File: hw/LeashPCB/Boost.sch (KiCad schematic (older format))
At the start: 38 parts, among them U1001 TPS62821DLC, U1002 TPS61026, U1003 TPS61025

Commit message: Added antenna and routed ideal diode circuit
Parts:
- removed JP801, JP802, JP804, JP805, JP806: SolderJumper_2_Bridged, Jumper:SolderJumper-2_P1.3mm_Bridged2Bar_RoundedPad1.0x1.5mm, symbol Jumper:SolderJumper_2_Bridged
- removed JP803: SolderJumper_2_Open, Jumper:SolderJumper-2_P1.3mm_Open_RoundedPad1.0x1.5mm, symbol Jumper:SolderJumper_2_Open
- added R10, R9: 0, Resistor_SMD:R_0402_1005Metric, symbol Device:R
- C1003, C1007, L1003, R1008, R1014, R1015, U1001: Population (none) -> DNP
- C1009: footprint Capacitor_SMD:C_0402_1005Metric -> Capacitor_SMD:C_0603_1608Metric; Population (none) -> DNP
- R1017: Population DNP -> (none)
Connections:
- net labels added: +3V3, +5V, 3V3_BOOST_VOUT, 3V3_BUCK_VOUT, 5V_BOOST_VOUT
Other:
- note added: "Not normally populated"
- moved on the sheet: C1003, C1007, C1009, L1003, R1008, R1014, R1015

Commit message: Pulled in final small components and finished routing all but the RF section
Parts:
- added JP801, JP802, JP803, JP804, JP805: SolderJumper_2_Bridged, Jumper:SolderJumper-2_P1.3mm_Bridged2Bar_RoundedPad1.0x1.5mm, symbol Jumper:SolderJumper_2_Bridged
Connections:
- wire segments 161 -> 166
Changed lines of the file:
@@
 $EndComp
 Connection ~ 8800 7500
-Text HLabel 2125 2100 0    98   Input ~ 0
+Text HLabel 1475 2100 0    98   Input ~ 0
 V_BAT
-Text HLabel 2125 2375 0    98   Input ~ 0
+Text HLabel 1475 2375 0    98   Input ~ 0
 V_ALT
 Wire Wire Line
 	3775 7500 4725 7500
-Text HLabel 2125 2675 0    98   Input ~ 0
+Text HLabel 1475 2675 0    98   Input ~ 0
 V_USB
 Text HLabel 10025 2925 2    118  Input ~ 0
@@
 3V3_REG
 Wire Wire Line
-	2125 2100 2600 2100
-Wire Wire Line
-	2125 2375 2300 2375
-Wire Wire Line
 	3100 2375 3100 2100
 Connection ~ 3100 2100
@@
 	3100 2100 3250 2100
 Wire Wire Line
-	2125 2675 2450 2675
-Wire Wire Line
 	3250 2675 3250 2100
 Connection ~ 3250 2100
-Wire Wire Line
-	2300 4875 2450 4875
-Connection ~ 2450 4875
-Wire Wire Line
-	2450 4875 2600 4875
 Text Notes 2975 3875 0    98   ~ 0
 V_Bat not hooked into \n5V output normally
@@
 Text Label 2925 4875 0    50   ~ 0
 5V_BOOST_VIN
-Connection ~ 2300 2375
-Connection ~ 2450 2675
 Connection ~ 2600 2100
 Wire Wire Line
@@
 Wire Wire Line
 	13800 4600 14150 4600
-Wire Wire Line
-	2450 2675 2450 4875
-Wire Wire Line
-	2300 2375 2300 4875
 $Comp
 L Device:R R10
@@
 $EndComp
 Wire Wire Line
-	2600 2100 3100 2100
-Wire Wire Line
-	2300 2375 3100 2375
-Wire Wire Line
-	2450 2675 3250 2675
+	2600 2100 2675 2100
 Wire Notes Line
 	10375 6850 10375 8875
@@
 Text Notes 5775 9025 0    98   ~ 0
 Not normally populated
+Wire Wire Line
+	2325 2375 2325 4050
+Connection ~ 2325 2375
+Wire Wire Line
+	2325 2375 2675 2375
+Wire Wire Line
+	2325 4875 2475 4875
+Wire Wire Line
+	2475 2675 2475 3750
+Connection ~ 2475 2675
+Wire Wire Line
+	2475 2675 2675 2675
+Connection ~ 2475 4875
+Wire Wire Line
+	2475 4875 2600 4875
+$Comp
+L Jumper:SolderJumper_2_Bridged JP803
+U 1 1 5D5C1D3B
+P 2825 2100
+F 0 "JP803" H 2825 2213 50  0000 C CNN
+F 1 "SolderJumper_2_Bridged" H 2825 2214 50  0001 C CNN
+F 2 "Jumper:SolderJumper-2_P1.3mm_Bridged2Bar_RoundedPad1.0x1.5mm" H 2825 2100 50  0001 C CNN
+F 3 "~" H 2825 2100 50  0001 C CNN
+	1    2825 2100
+	1    0    0    -1
+$EndComp
+$Comp
+L Jumper:SolderJumper_2_Bridged JP804
+U 1 1 5D5CEF43
+P 2825 2375
+F 0 "JP804" H 2825 2488 50  0000 C CNN
+F 1 "SolderJumper_2_Bridged" H 2825 2489 50  0001 C CNN
+F 2 "Jumper:SolderJumper-2_P1.3mm_Bridged2Bar_RoundedPad1.0x1.5mm" H 2825 2375 50  0001 C CNN
+F 3 "~" H 2825 2375 50  0001 C CNN
+	1    2825 2375
+	1    0    0    -1
+$EndComp
+$Comp
+L Jumper:SolderJumper_2_Bridged JP805
+U 1 1 5D5CF3F5
+P 2825 2675
+F 0 "JP805" H 2825 2788 50  0000 C CNN
+F 1 "SolderJumper_2_Bridged" H 2825 2789 50  0001 C CNN
+F 2 "Jumper:SolderJumper-2_P1.3mm_Bridged2Bar_RoundedPad1.0x1.5mm" H 2825 2675 50  0001 C CNN
+F 3 "~" H 2825 2675 50  0001 C CNN
+	1    2825 2675
+	1    0    0    -1
+$EndComp
+$Comp
+L Jumper:SolderJumper_2_Bridged JP802
+U 1 1 5D5CFDCF
+P 2475 3900
+F 0 "JP802" V 2475 4100 50  0000 L CNN
+F 1 "SolderJumper_2_Bridged" H 2475 4014 50  0001 C CNN
+F 2 "Jumper:SolderJumper-2_P1.3mm_Bridged2Bar_RoundedPad1.0x1.5mm" H 2475 3900 50  0001 C CNN
+F 3 "~" H 2475 3900 50  0001 C CNN
+	1    2475 3900
+	0    1    1    0
+$EndComp
+Wire Wire Line
+	2475 4050 2475 4875
+$Comp
+L Jumper:SolderJumper_2_Bridged JP801
+U 1 1 5D5D22C0
+P 2325 4200
+F 0 "JP801" V 2325 4525 50  0000 L CNN
+F 1 "SolderJumper_2_Bridged" H 2325 4314 50  0001 C CNN
+F 2 "Jumper:SolderJumper-2_P1.3mm_Bridged2Bar_RoundedPad1.0x1.5mm" H 2325 4200 50  0001 C CNN
+F 3 "~" H 2325 4200 50  0001 C CNN
+	1    2325 4200
+	0    1    1    0
+$EndComp
+Wire Wire Line
+	2325 4350 2325 4875
+Text Label 1625 2675 0    50   ~ 0
+V_USB
+Text Label 1625 2375 0    50   ~ 0
+V_ALT
+Text Label 1625 2100 0    50   ~ 0
+V_BAT
+Wire Wire Line
+	2975 2100 3100 2100
+Wire Wire Line
+	2975 2375 3100 2375
+Wire Wire Line
+	2975 2675 3250 2675
+Wire Wire Line
+	1475 2100 2600 2100
+Wire Wire Line
+	1475 2375 2325 2375
+Wire Wire Line
+	1475 2675 2475 2675
 $EndSCHEMATC

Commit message: Added a swtich for future testing that would allow us to remove the ideal diode controller
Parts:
- added R? (x3): 0, Resistor_SMD:R_0402_1005Metric, symbol Device:R
- added SW?: SW_SPDT, symbol Switch:SW_SPDT
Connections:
- wire segments 166 -> 181
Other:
- note added: "Adding in a low cost, small switch for\nfuture cost reduction. Removes the need\nfor ideal diode controller."
- note added: "CONFIG 1: All power inputs go into 3V3 boost, ALT and USB go into the 5V boost\nCONFIG 2: All power inputs go into 3V3 boost, all go into the 5V boost\nCONFIG 3: All power inputs go into 5V boost, 5V is bucked down to 3V3\nCONFIG 4: User has to manually swich from internal power to external power, which are diode ORed together"
- note removed: "CONFIG 1: All power inputs go into 3V3 boost, ALT and USB go into the 5V boost\nCONFIG 2: All power inputs go into 3V3 boost, all go into the 5V boost\nCONFIG 3: All power inputs go into 5V boost, 5V is bucked down to 3V3"
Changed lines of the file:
@@
 Connection ~ 2600 4875
 Text Notes 4425 1225 0    98   ~ 0
-CONFIG 1: All power inputs go into 3V3 boost, ALT and USB go into the 5V boost\nCONFIG 2: All power inputs go into 3V3 boost, all go into the 5V boost\nCONFIG 3: All power inputs go into 5V boost, 5V is bucked down to 3V3
+CONFIG 1: All power inputs go into 3V3 boost, ALT and USB go into the 5V boost\nCONFIG 2: All power inputs go into 3V3 boost, all go into the 5V boost\nCONFIG 3: All power inputs go into 5V boost, 5V is bucked down to 3V3\nCONFIG 4: User has to manually swich from internal power to external power, which are diode ORed together
 Wire Wire Line
 	12825 2000 12825 3175
@@
 Connection ~ 2600 2100
 Wire Wire Line
-	3250 2100 4525 2100
-Wire Wire Line
-	2600 4875 4725 4875
+	3250 2100 4325 2100
+Wire Wire Line
+	2600 4875 3775 4875
 Connection ~ 4725 4875
 Wire Wire Line
@@
 Wire Wire Line
 	1475 2675 2475 2675
+$Comp
+L Switch:SW_SPDT SW?
+U 1 1 5D429FC4
+P 1925 5900
+F 0 "SW?" H 1925 5575 50  0000 C CNN
+F 1 "SW_SPDT" H 1925 5666 50  0000 C CNN
+F 2 "" H 1925 5900 50  0001 C CNN
+F 3 "~" H 1925 5900 50  0001 C CNN
+F 4 "K3-1293S-E2" H 1925 5900 50  0001 C CNN "MPN1"
+F 5 "DNP" H 1925 5900 50  0001 C CNN "Population"
+F 6 "https://lcsc.com/product-detail/Toggle-Switches_Korean-Hroparts-Elec-K3-1293S-E2_C145852.html" H 1925 5900 50  0001 C CNN "Link1"
+	1    1925 5900
+	-1   0    0    1
+$EndComp
+Wire Wire Line
+	2125 5900 3775 5900
+Wire Wire Line
+	3775 5900 3775 5700
+Connection ~ 3775 4875
+Wire Wire Line
+	3775 4875 4725 4875
+Wire Wire Line
+	3775 5900 4325 5900
+Wire Wire Line
+	4325 5900 4325 5725
+Connection ~ 3775 5900
+Connection ~ 4325 2100
+Wire Wire Line
+	4325 2100 4525 2100
+Wire Wire Line
+	1725 6000 750  6000
+Text Label 750  6000 0    50   ~ 0
+V_BAT
+Wire Wire Line
+	1725 5800 1475 5800
+Wire Wire Line
+	1475 5800 1475 5650
+$Comp
+L Device:R R?
+U 1 1 5D476FC0
+P 1250 5400
+F 0 "R?" H 1320 5491 50  0000 L CNN
+F 1 "0" H 1320 5400 50  0000 L CNN
+F 2 "Resistor_SMD:R_0402_1005Metric" V 1180 5400 50  0001 C CNN
+F 3 "~" H 1250 5400 50  0001 C CNN
+F 4 "DNP" H 1320 5309 50  0000 L CNN "Population"
+	1    1250 5400
+	0    1    1    0
+$EndComp
+Wire Wire Line
+	1400 5400 1475 5400
+Wire Wire Line
+	1475 5650 750  5650
+Connection ~ 1475 5650
+Wire Wire Line
+	1475 5650 1475 5400
+Wire Wire Line
+	1100 5400 750  5400
+Text Label 750  5650 0    50   ~ 0
+V_ALT
+Text Label 750  5400 0    50   ~ 0
+V_USB
+$Comp
+L Device:R R?
+U 1 1 5D4BC09C
+P 3775 5550
+F 0 "R?" H 3845 5641 50  0000 L CNN
+F 1 "0" H 3845 5550 50  0000 L CNN
+F 2 "Resistor_SMD:R_0402_1005Metric" V 3705 5550 50  0001 C CNN
+F 3 "~" H 3775 5550 50  0001 C CNN
+F 4 "DNP" H 3845 5459 50  0000 L CNN "Population"
+	1    3775 5550
+	-1   0    0    1
+$EndComp
+Wire Wire Line
+	3775 5400 3775 4875
+$Comp
+L Device:R R?
+U 1 1 5D4BCBD7
+P 4325 5575
+F 0 "R?" H 4395 5666 50  0000 L CNN
+F 1 "0" H 4395 5575 50  0000 L CNN
+F 2 "Resistor_SMD:R_0402_1005Metric" V 4255 5575 50  0001 C CNN
+F 3 "~" H 4325 5575 50  0001 C CNN
+F 4 "DNP" H 4395 5484 50  0000 L CNN "Population"
+	1    4325 5575
+	-1   0    0    1
+$EndComp
+Wire Wire Line
+	4325 5425 4325 2100
+Text Notes 1075 6525 0    79   ~ 0
+Adding in a low cost, small switch for\nfuture cost reduction. Removes the need\nfor ideal diode controller.
 $EndSCHEMATC

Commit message: Added a switch and finished closing out DRC errors. Added a lot of via stiching in RF section.
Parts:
- added R?: 0, Resistor_SMD:R_0402_1005Metric, symbol Device:R
- SW801: renamed from SW?; footprint (none) -> leash:K3-1293S-E2
- gave numbers to parts that had none: 3
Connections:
- wire segments 181 -> 187
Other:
- note added: "Optional pull up resistor\nto change to default on \nbehavior"
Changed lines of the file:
@@
 Connection ~ 5900 4975
 Wire Wire Line
-	5900 4975 5775 4975
+	5900 4975 5825 4975
 $Bitmap
 Pos 20325 5400
@@
 	1475 2675 2475 2675
 $Comp
-L Switch:SW_SPDT SW?
+L Switch:SW_SPDT SW801
 U 1 1 5D429FC4
 P 1925 5900
-F 0 "SW?" H 1925 5575 50  0000 C CNN
+F 0 "SW801" H 1925 5575 50  0000 C CNN
 F 1 "SW_SPDT" H 1925 5666 50  0000 C CNN
-F 2 "" H 1925 5900 50  0001 C CNN
-F 3 "~" H 1925 5900 50  0001 C CNN
+F 2 "leash:K3-1293S-E2" H 1925 5900 50  0001 C CNN
+F 3 "https://datasheet.lcsc.com/szlcsc/Korean-Hroparts-Elec-K3-1293S-E2_C145852.pdf" H 1925 5900 50  0001 C CNN
 F 4 "K3-1293S-E2" H 1925 5900 50  0001 C CNN "MPN1"
 F 5 "DNP" H 1925 5900 50  0001 C CNN "Population"
 F 6 "https://lcsc.com/product-detail/Toggle-Switches_Korean-Hroparts-Elec-K3-1293S-E2_C145852.html" H 1925 5900 50  0001 C CNN "Link1"
 	1    1925 5900
-	-1   0    0    1
+	-1   0    0    -1
 $EndComp
 Wire Wire Line
@@
 Connection ~ 3775 4875
 Wire Wire Line
-	3775 4875 4725 4875
+	3775 4875 4575 4875
 Wire Wire Line
 	3775 5900 4325 5900
@@
 	1475 5800 1475 5650
 $Comp
-L Device:R R?
+L Device:R R801
 U 1 1 5D476FC0
 P 1250 5400
-F 0 "R?" H 1320 5491 50  0000 L CNN
+F 0 "R801" H 1320 5491 50  0000 L CNN
 F 1 "0" H 1320 5400 50  0000 L CNN
 F 2 "Resistor_SMD:R_0402_1005Metric" V 1180 5400 50  0001 C CNN
@@
 V_USB
 $Comp
-L Device:R R?
+L Device:R R802
 U 1 1 5D4BC09C
 P 3775 5550
-F 0 "R?" H 3845 5641 50  0000 L CNN
+F 0 "R802" H 3845 5641 50  0000 L CNN
 F 1 "0" H 3845 5550 50  0000 L CNN
 F 2 "Resistor_SMD:R_0402_1005Metric" V 3705 5550 50  0001 C CNN
@@
 	3775 5400 3775 4875
 $Comp
-L Device:R R?
+L Device:R R803
 U 1 1 5D4BCBD7
 P 4325 5575
-F 0 "R?" H 4395 5666 50  0000 L CNN
+F 0 "R803" H 4395 5666 50  0000 L CNN
 F 1 "0" H 4395 5575 50  0000 L CNN
 F 2 "Resistor_SMD:R_0402_1005Metric" V 4255 5575 50  0001 C CNN
@@
 Wire Wire Line
 	4325 5425 4325 2100
-Text Notes 1075 6525 0    79   ~ 0
+Text Notes 950  6625 0    79   ~ 0
 Adding in a low cost, small switch for\nfuture cost reduction. Removes the need\nfor ideal diode controller.
+$Comp
+L Device:R R?
+U 1 1 5D45EB51
+P 5825 4525
+F 0 "R?" H 5895 4616 50  0000 L CNN
+F 1 "0" H 5895 4525 50  0000 L CNN
+F 2 "Resistor_SMD:R_0402_1005Metric" V 5755 4525 50  0001 C CNN
+F 3 "~" H 5825 4525 50  0001 C CNN
+F 4 "DNP" H 5895 4434 50  0000 L CNN "Population"
+	1    5825 4525
+	-1   0    0    1
+$EndComp
+Wire Wire Line
+	5825 4675 5825 4975
+Connection ~ 5825 4975
+Wire Wire Line
+	5825 4975 5775 4975
+Wire Wire Line
+	4575 4875 4575 4250
+Wire Wire Line
+	4575 4250 5825 4250
+Wire Wire Line
+	5825 4250 5825 4375
+Connection ~ 4575 4875
+Wire Wire Line
+	4575 4875 4725 4875
+Text Notes 5875 4300 0    50   ~ 0
+Optional pull up resistor\nto change to default on \nbehavior
 $EndSCHEMATC

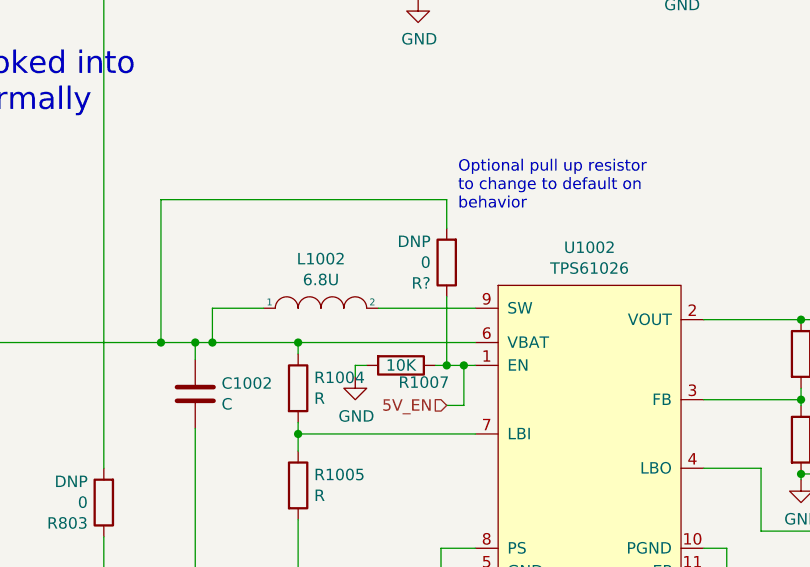
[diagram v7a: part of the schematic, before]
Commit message: Hooked up RX/TX to the USB converter (whoops) and added a few other small connections.
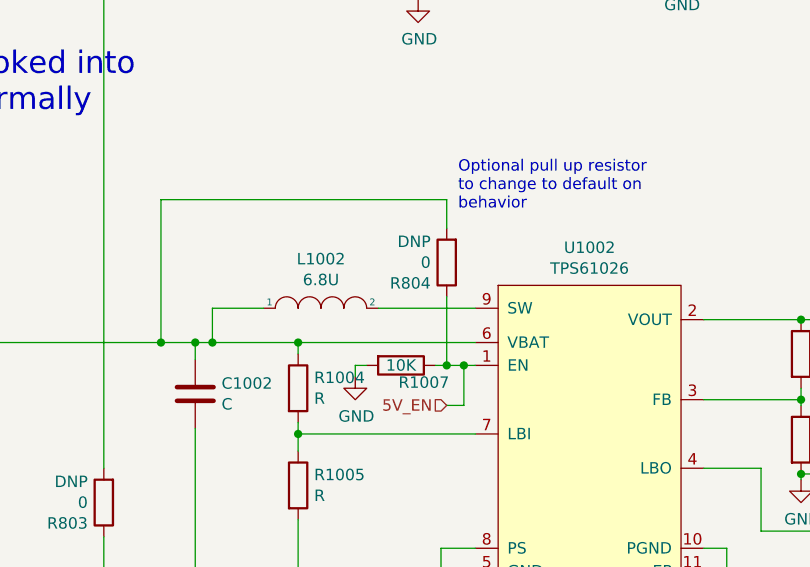
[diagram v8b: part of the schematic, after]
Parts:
- SW801: Value modifier (none) -> Alt #: JS102011SAQN
- gave numbers to parts that had none: 1
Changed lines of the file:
@@
 Text HLabel 1475 2675 0    98   Input ~ 0
 V_USB
-Text HLabel 10025 2925 2    118  Input ~ 0
-3v3_CTRL
-Wire Wire Line
-	8275 2925 10025 2925
 Wire Wire Line
 	7000 2925 8275 2925
-Connection ~ 8275 2925
 Wire Wire Line
 	8275 2500 8275 2925
@@
 F 5 "DNP" H 1925 5900 50  0001 C CNN "Population"
 F 6 "https://lcsc.com/product-detail/Toggle-Switches_Korean-Hroparts-Elec-K3-1293S-E2_C145852.html" H 1925 5900 50  0001 C CNN "Link1"
+F 7 "Alt #: JS102011SAQN" H 1925 5900 50  0001 C CNN "Value modifier"
 	1    1925 5900
 	-1   0    0    -1
@@
 Adding in a low cost, small switch for\nfuture cost reduction. Removes the need\nfor ideal diode controller.
 $Comp
-L Device:R R?
+L Device:R R804
 U 1 1 5D45EB51
 P 5825 4525
-F 0 "R?" H 5895 4616 50  0000 L CNN
+F 0 "R804" H 5895 4616 50  0000 L CNN
 F 1 "0" H 5895 4525 50  0000 L CNN
 F 2 "Resistor_SMD:R_0402_1005Metric" V 5755 4525 50  0001 C CNN
@@
 Text Notes 5875 4300 0    50   ~ 0
 Optional pull up resistor\nto change to default on \nbehavior
+Connection ~ 8275 2925
+Wire Wire Line
+	8275 2925 10025 2925
+Text HLabel 10025 2925 2    118  Input ~ 0
+3v3_CTRL
 $EndSCHEMATC
